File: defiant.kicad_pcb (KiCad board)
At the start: 2 copper layers, 126.6 x 99.6 mm, 55 parts, among them J1 Conn_01x02_Pin, SW1 SW_Push, SW2 SW_Push, SW3 SW_DP3T, T0 SW_PUSH, T1 SW_PUSH, T2 SW_PUSH, T3 SW_PUSH, T4 SW_PUSH, U1 Seeed Studio XIAO BLE

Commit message: Experimental: Tighten thumb key placing
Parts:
- moved T4 1.78 mm to (190.6, 134.3)
- moved D20 1.78 mm to (192.9, 129.5)
- moved T3 1.65 mm to (171.8, 124.3)
- moved D16 1.65 mm to (172.8, 119.1)
- moved C0R1 1.09 mm to (89.2, 70.8)
- moved D14 1.09 mm to (145.3, 76.6)
- moved D8 1.09 mm to (128.7, 114.6)
- moved REF** 1.09 mm to (117.7, 91.3)
- moved C1R1 1.09 mm to (108.2, 62.8)
- moved C2R2 1.09 mm to (127.2, 77.8)
- moved C2R3 1.09 mm to (127.2, 96.8)
- moved D1 1.09 mm to (88.3, 65.6)
- moved D3 1.09 mm to (88.3, 103.6)
- moved J1 1.09 mm to (199.7, 88.4)
- moved D9 1.09 mm to (126.3, 53.6)
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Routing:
- net row3: track 107.0 -> 105.5 mm
- net col4: track 155.7 -> 156.8 mm
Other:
- board size 126.6 x 99.6 mm -> 126.6 x 99.2 mm

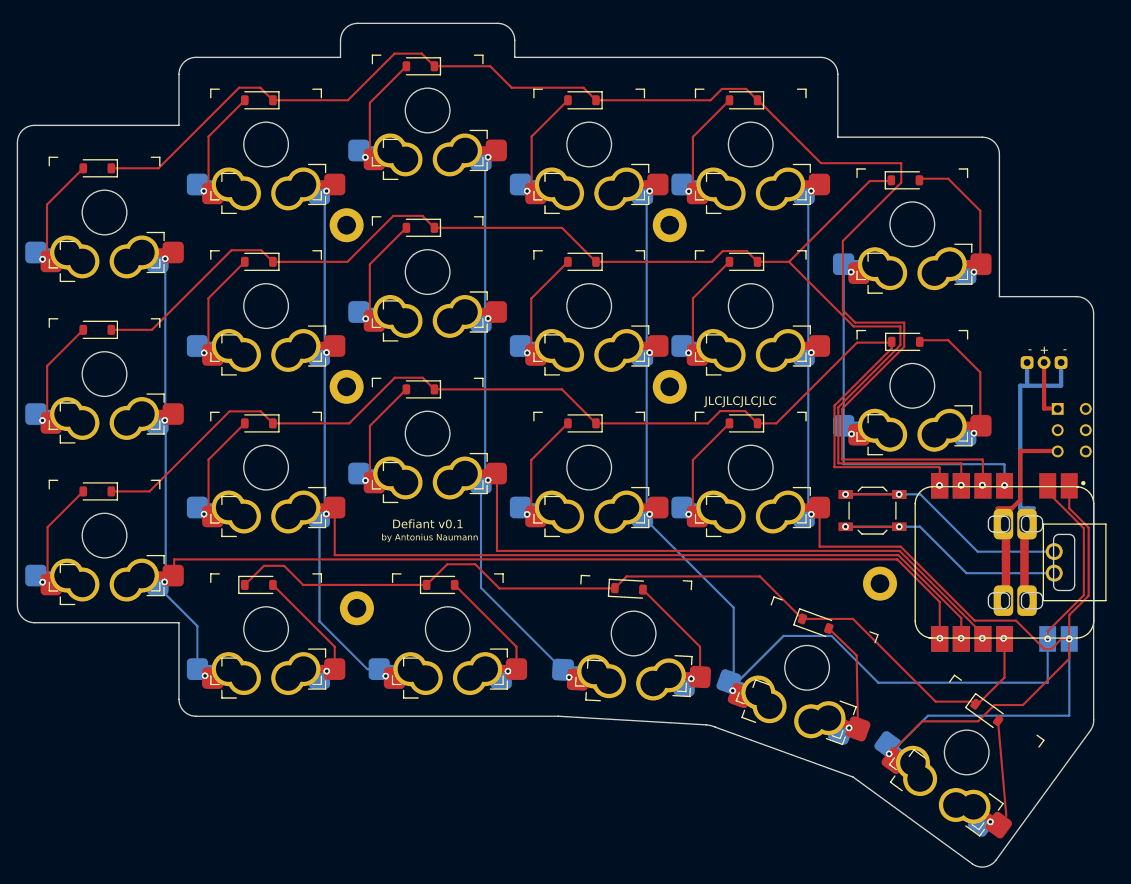
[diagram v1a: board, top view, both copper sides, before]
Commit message: Move pinky column down by 1mm
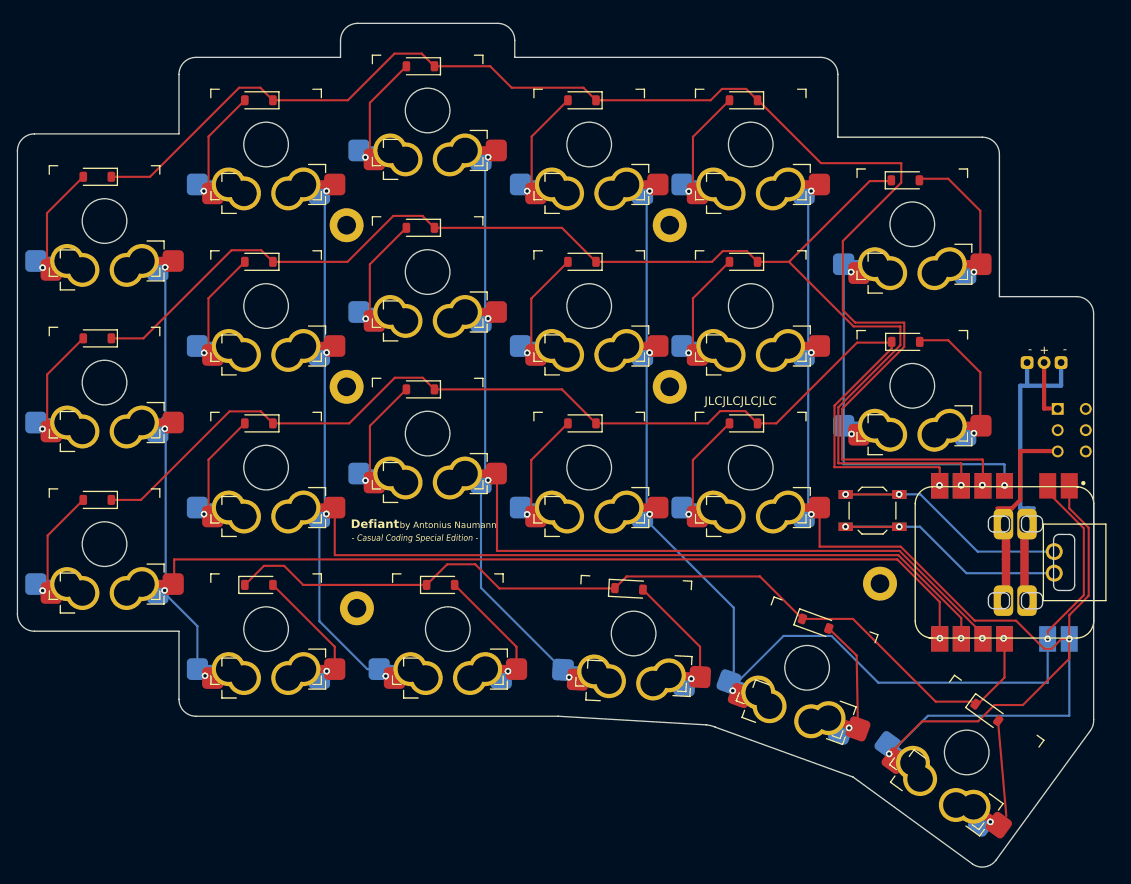
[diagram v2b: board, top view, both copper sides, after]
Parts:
- moved C0R1 1.00 mm to (89.2, 71.8)
- moved C0R2 1.00 mm to (89.2, 90.8)
- moved C0R3 1.00 mm to (89.2, 109.8)
- moved D1 1.00 mm to (88.3, 66.6)
- moved D2 1.00 mm to (88.3, 85.6)
- moved D3 1.00 mm to (88.3, 104.6)
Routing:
- net col0: track 149.5 -> 150.1 mm
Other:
- outline, holes or cut-outs redrawn
- board text added: "- Casual Coding Special Edition -"
- board text added: "Defiant"
- board text removed: "Defiant v0.1"
- board text removed: "Mik Müller Special Edition"

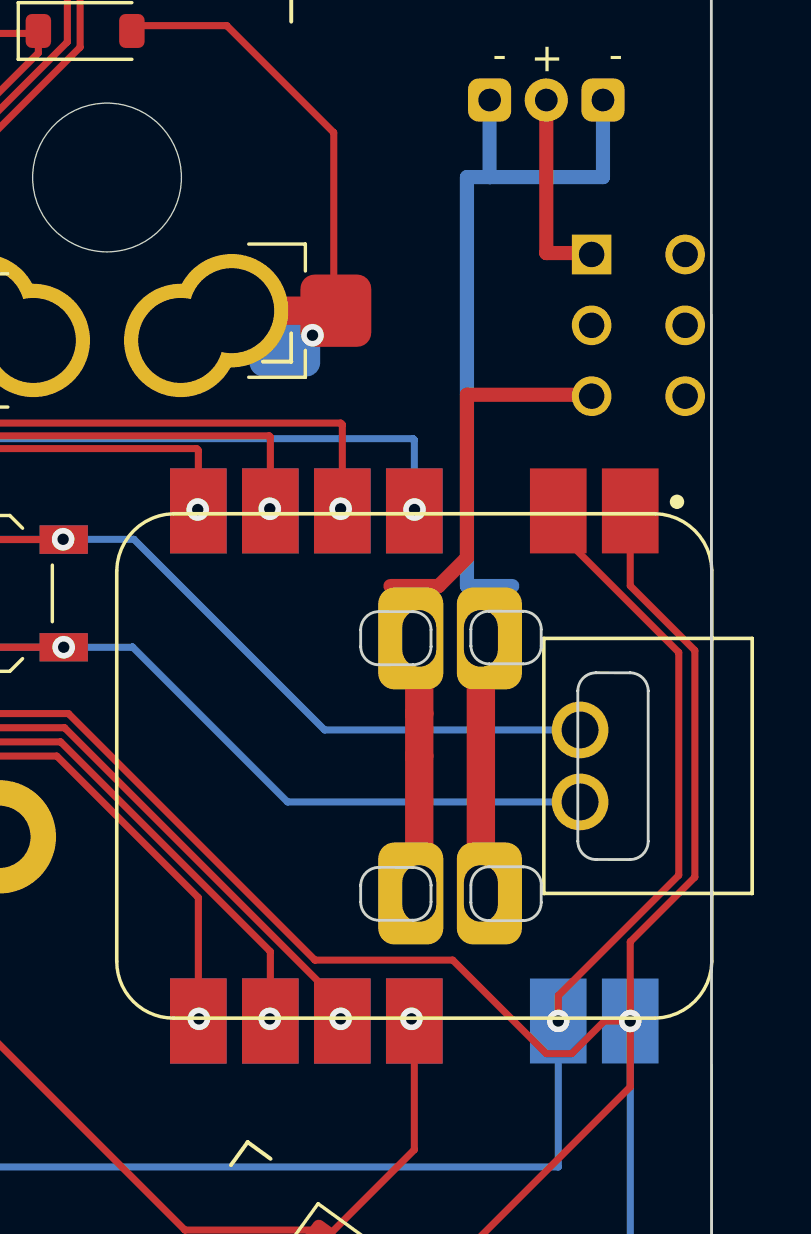
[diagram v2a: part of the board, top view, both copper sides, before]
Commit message: Replace XIAO BLE handsolder footprint with SMD solder footprint
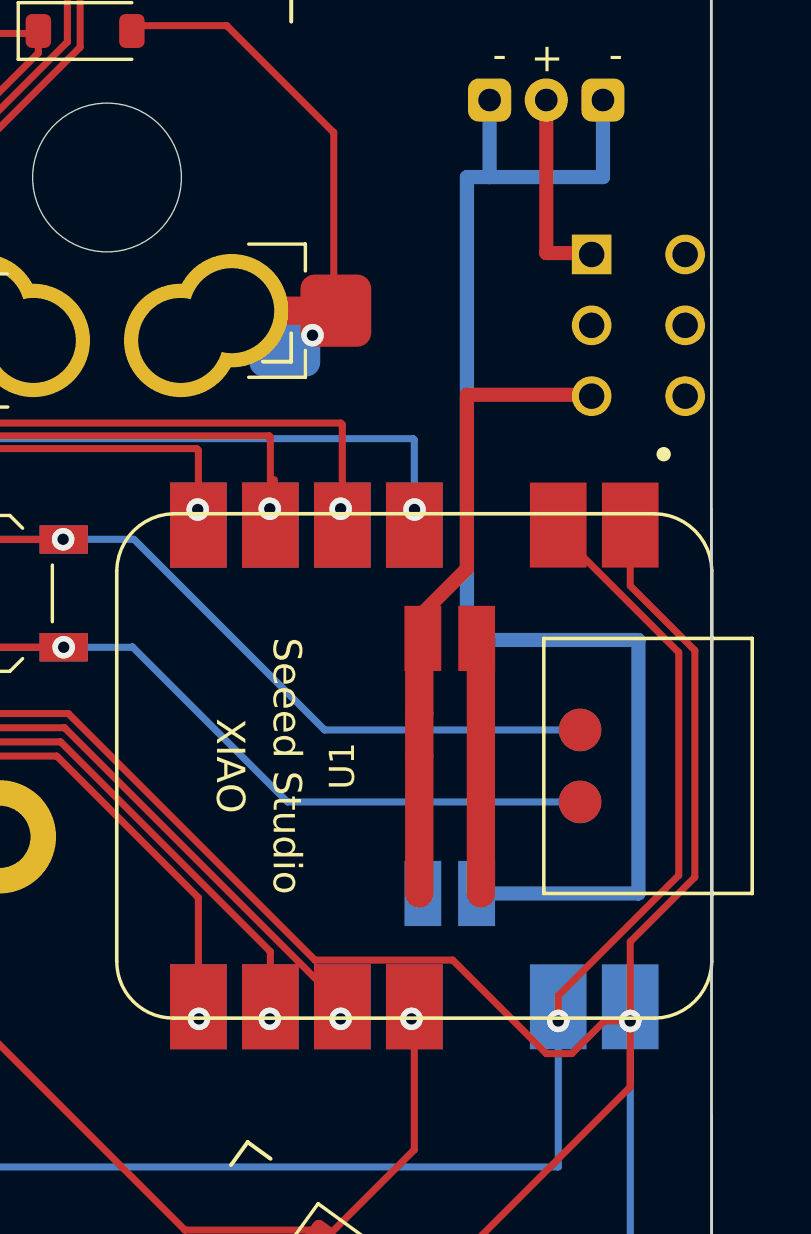
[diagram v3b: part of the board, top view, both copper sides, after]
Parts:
- U1: footprint Seeedstudio XIAO:XIAO-nRF52840-Sense-14P-2.54-21X17.8MM_NoLED_Handsolder -> Seeedstudio XIAO:XIAO-nRF52840-Sense-14P-2.54-21X17.8MM_Reduced_Pins
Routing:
- net Net-(J1-Pin_1): track 36.5 -> 56.3 mm

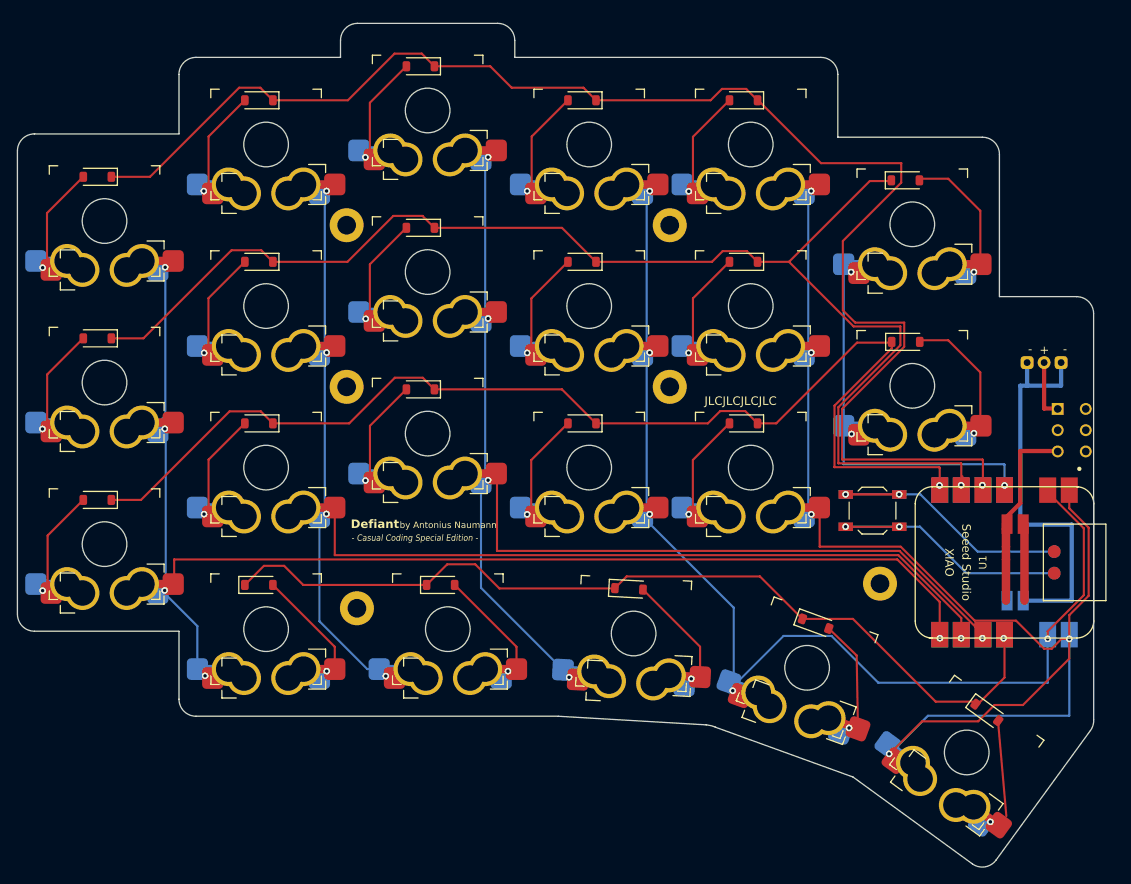
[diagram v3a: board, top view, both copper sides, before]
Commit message: Change pcb lane width to 0.4mm
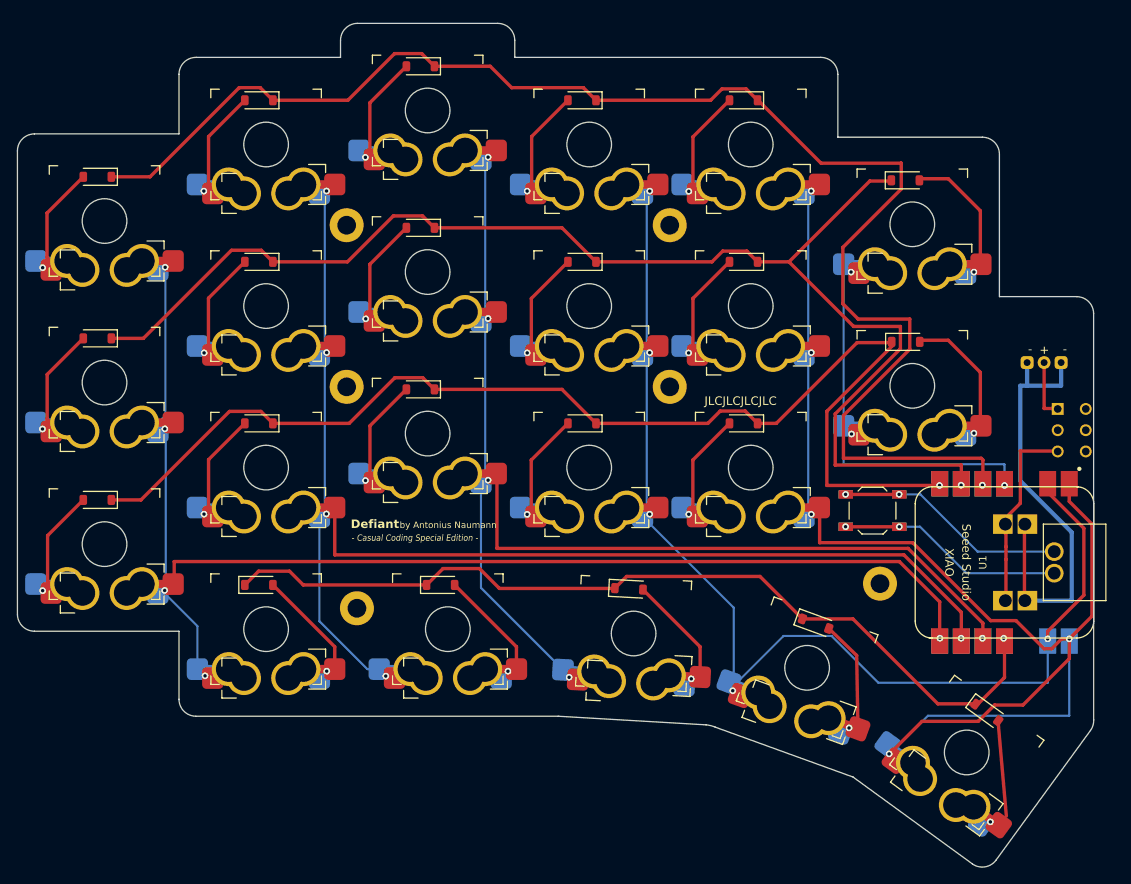
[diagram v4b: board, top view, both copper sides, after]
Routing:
- net Net-(J1-Pin_1): track 56.3 -> 52.7 mm
- net row2: track 138.3 -> 139.5 mm
- net col2: track 134.9 -> 135.5 mm
- net row3: track 105.5 -> 105.0 mm
- net Net-(U1-BAT+): track 23.4 -> 22.8 mm
- net row1: track 160.0 -> 160.6 mm

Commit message: Move vias out of pads
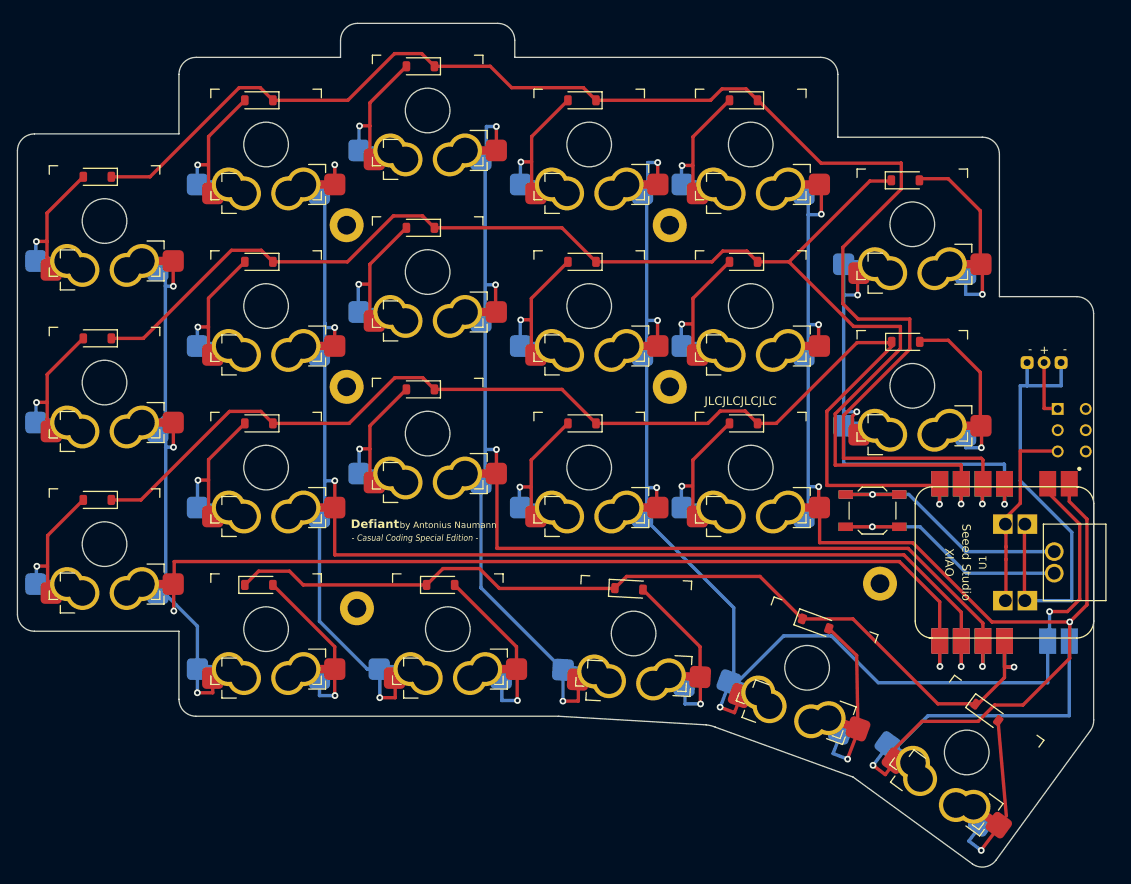
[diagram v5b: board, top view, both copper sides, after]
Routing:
- net col2: track 135.5 -> 162.0 mm
- net col1: track 144.9 -> 170.8 mm
- net col0: track 149.7 -> 173.8 mm
- net col3: track 130.3 -> 151.6 mm
- net col4: track 156.8 -> 175.3 mm
- net col5: track 45.0 -> 58.9 mm
- net Net-(D22-A): track 16.0 -> 24.1 mm
- net Net-(D4-A): track 12.9 -> 19.9 mm
- net Net-(D20-A): track 11.2 -> 18.2 mm
- net Net-(D12-A): track 13.1 -> 20.0 mm
- net Net-(D8-A): track 12.9 -> 19.9 mm
- net Net-(D16-A): track 13.2 -> 20.2 mm
- net Net-(D23-A): track 15.9 -> 21.9 mm
- net row3: track 105.0 -> 110.3 mm
- net row2: track 139.5 -> 144.3 mm
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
